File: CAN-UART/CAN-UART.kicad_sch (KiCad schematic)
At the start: 19 parts, among them CN1 1.0T-4PLTPZ, J1 Conn_01x06, P1 USB_C_Plug_USB2.0, U1 AP2112K-3.3, U2 SN65HVD230, U3 ESP32-C3, U4 AT45DB161D-SU

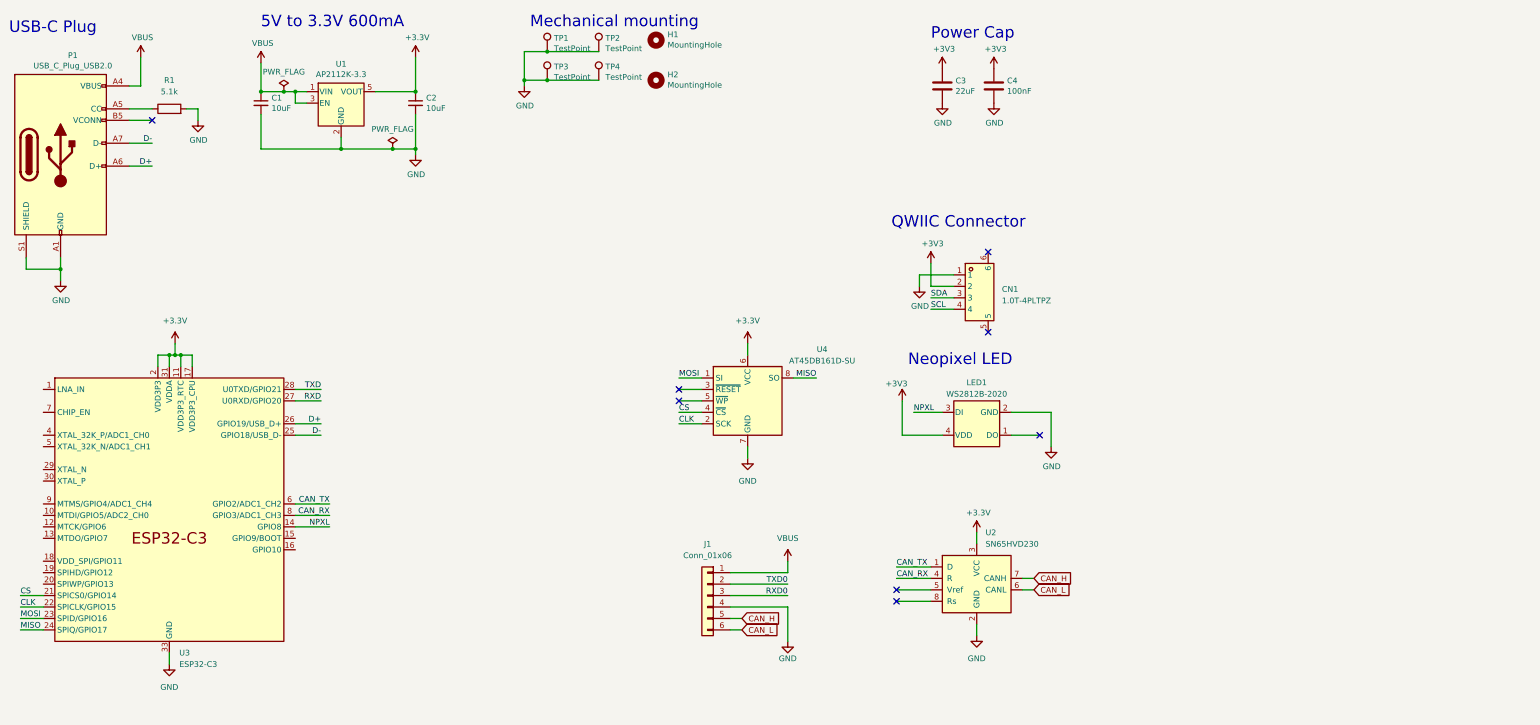
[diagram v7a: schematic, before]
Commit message: Reorder Schematic
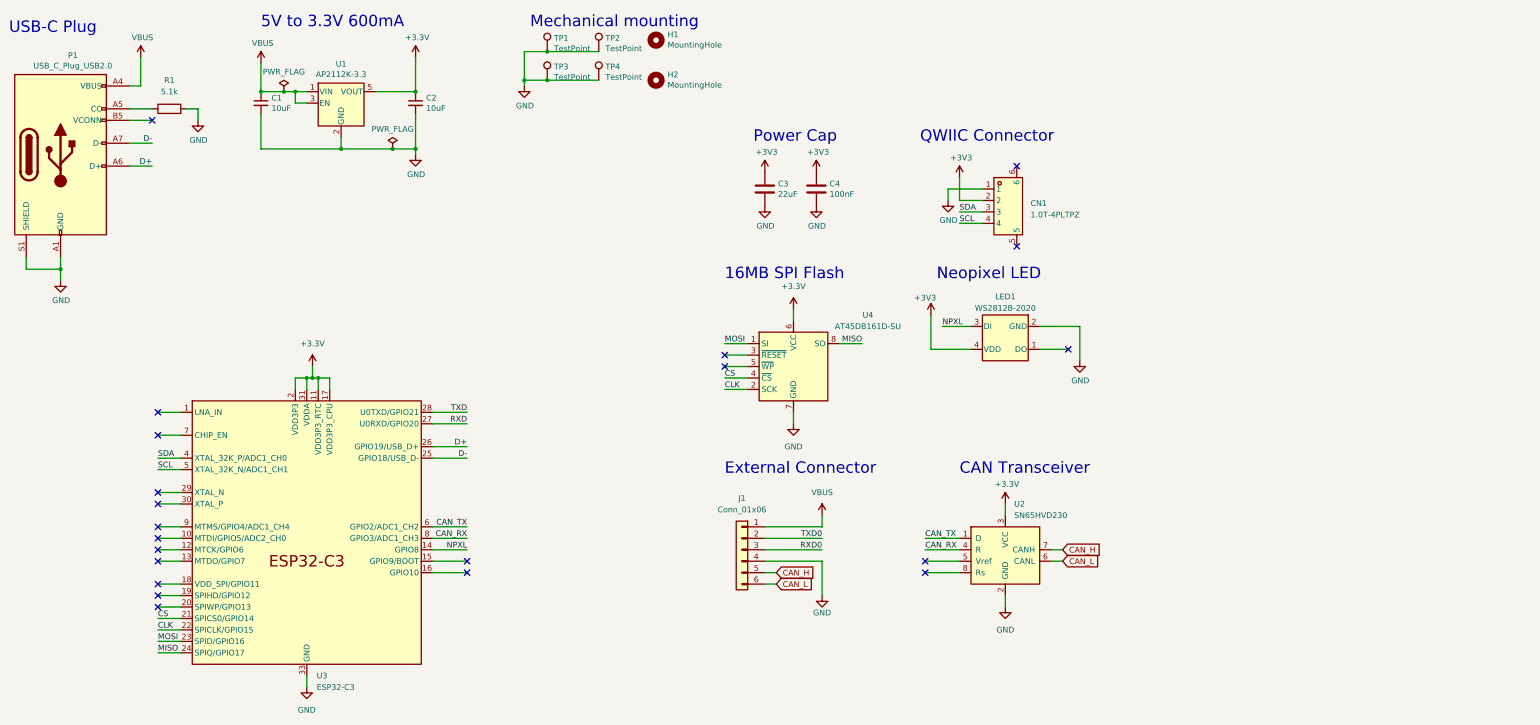
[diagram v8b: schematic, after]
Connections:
- net SCL: now also U3.5 (XTAL_32K_N/ADC1_CH1)
- net SDA: now also U3.4 (XTAL_32K_P/ADC1_CH0)
- no-connect marks 8 -> 21
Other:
- note added: "16MB SPI Flash"
- note added: "CAN Transceiver"
- note added: "External Connector"
- moved on the sheet: C3, C4, CN1, J1, LED1, U2, U3, U4
